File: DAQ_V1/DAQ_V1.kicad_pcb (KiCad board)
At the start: 2 copper layers, 105 x 98 mm, 18 parts, among them J2 Conn_01x04_Socket, J3 Conn_01x04_Socket, J4 Conn_01x04_Socket, J5 Conn_01x04_Socket

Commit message: Updated PCB design
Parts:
- added G***: LOGO, CustomLibrary:SHIFU_SS, F.Cu at (161.0, 93.0)
- A2: footprint PCM_arduino-library:Arduino_Mega2560_R3_Shield -> CustomLibrary:Arduino_Mega2560_R3_Shield_custom
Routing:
- net Net-(J2-Pin_1): track 112.7 -> 114.7 mm
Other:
- board text added: "Adafruit MAX31856"
- board text added: "MT3608"
- board text added: "Mega 2560"
- board text added: "SHIFU V1 - Sensing Heat & Intense Fluid Uh-ohs"

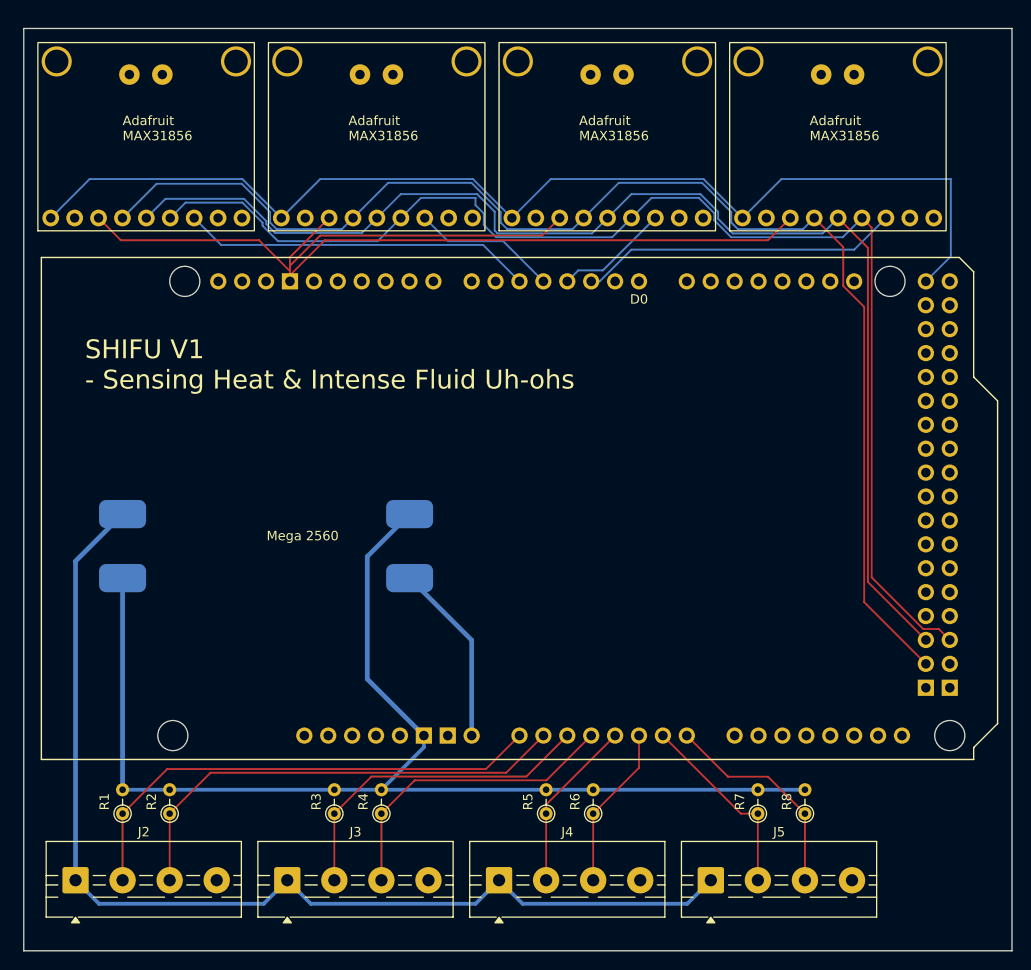
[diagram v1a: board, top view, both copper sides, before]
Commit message: V1.1 Updated design for bottom arduino mounting
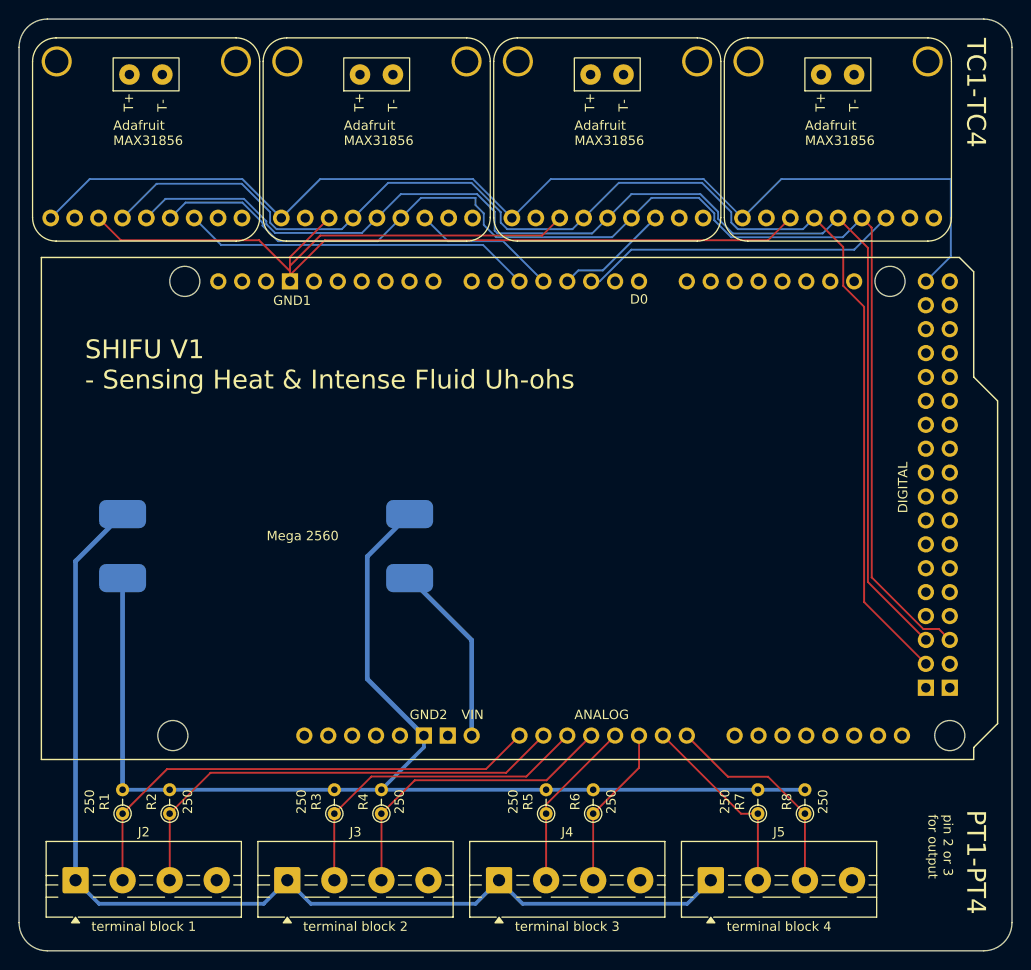
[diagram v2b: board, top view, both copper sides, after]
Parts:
- J2: value Conn_01x04_Socket -> terminal block 1
- J3: value Conn_01x04_Socket -> terminal block 2
- J4: value Conn_01x04_Socket -> terminal block 3
- J5: value Conn_01x04_Socket -> terminal block 4
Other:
- board size 105 x 98 mm -> 105.5 x 99 mm
- board text added: "ANALOG"
- board text added: "DIGITAL"
- board text added: "GND1"
- board text added: "GND2"
- board text added: "HIGH V"
- board text added: "LOW V"
- board text added: "PT1-PT4"
- board text added: "TC1-TC4"
- board text added: "VIN"
- board text added: "pin 2 or 3 for output"
